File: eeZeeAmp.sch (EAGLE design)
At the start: 18 parts, among them IC1 LM386

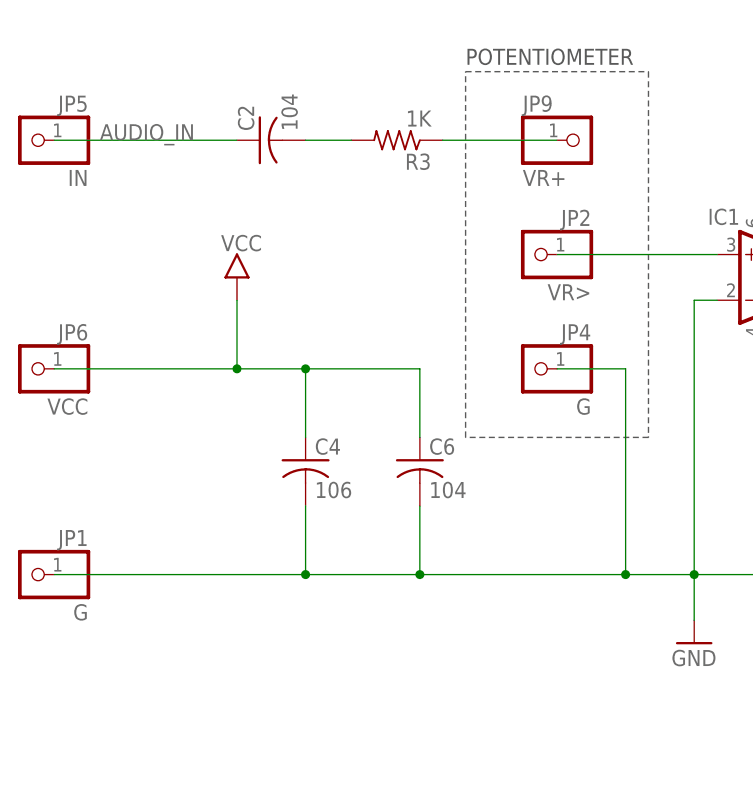
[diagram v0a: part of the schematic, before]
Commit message: Added another ground pin, rearrange layout
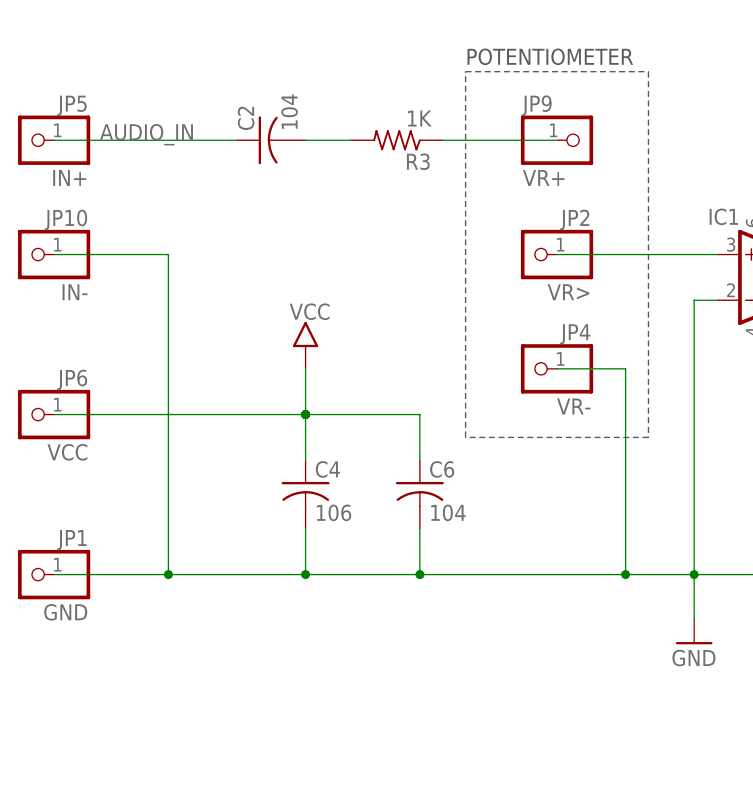
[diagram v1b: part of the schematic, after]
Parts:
- added JP10: IN-, pinhead-2:PINHD-1X01_2.54-S
- JP1: value G -> GND
- JP4: value G -> VR-
- JP5: value IN -> IN+
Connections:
- net GND: now also JP10.1
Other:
- moved on the sheet: C4, C6, JP6
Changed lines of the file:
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@@
 <part name="FRAME1" library="bt" deviceset="LETTER_L" device=""/>
 <part name="C6" library="rcl" deviceset="C-US" device="C0603" value="104"/>
-<part name="JP5" library="pinhead-2" deviceset="PINHD-1X01" device="_2.54-S" value="IN"/>
+<part name="JP5" library="pinhead-2" deviceset="PINHD-1X01" device="_2.54-S" value="IN+"/>
 <part name="JP6" library="pinhead-2" deviceset="PINHD-1X01" device="_2.54-S" value="VCC"/>
 <part name="JP7" library="pinhead-2" deviceset="PINHD-1X01" device="_2.54-S" value="SP+"/>
-<part name="JP1" library="pinhead-2" deviceset="PINHD-1X01" device="_2.54-S" value="G"/>
+<part name="JP1" library="pinhead-2" deviceset="PINHD-1X01" device="_2.54-S" value="GND"/>
 <part name="JP3" library="pinhead-2" deviceset="PINHD-1X01" device="_2.54-S" value="G1"/>
 <part name="JP8" library="pinhead-2" deviceset="PINHD-1X01" device="_2.54-S" value="G8"/>
-<part name="JP4" library="pinhead-2" deviceset="PINHD-1X01" device="_2.54-S" value="G"/>
+<part name="JP4" library="pinhead-2" deviceset="PINHD-1X01" device="_2.54-S" value="VR-"/>
 <part name="JP2" library="pinhead-2" deviceset="PINHD-1X01" device="_2.54-S" value="VR&gt;"/>
 <part name="JP9" library="pinhead-2" deviceset="PINHD-1X01" device="_2.54-S" value="VR+"/>
+<part name="JP10" library="pinhead-2" deviceset="PINHD-1X01" device="_2.54-S" value="IN-"/>
 </parts>
 <sheets>
@@
 <instance part="R3" gate="G$1" x="91.44" y="127" rot="R180"/>
 <instance part="U$1" gate="G$1" x="132.08" y="142.24"/>
-<instance part="U$2" gate="G$1" x="73.66" y="109.22"/>
-<instance part="C4" gate="G$1" x="81.28" y="91.44"/>
+<instance part="U$2" gate="G$1" x="81.28" y="101.6"/>
+<instance part="C4" gate="G$1" x="81.28" y="88.9"/>
 <instance part="GND1" gate="1" x="124.46" y="71.12"/>
 <instance part="C5" gate="G$1" x="137.16" y="96.52"/>
 <instance part="FRAME1" gate="G$1" x="0" y="0"/>
 <instance part="FRAME1" gate="G$2" x="147.32" y="2.54"/>
-<instance part="C6" gate="G$1" x="93.98" y="91.44"/>
+<instance part="C6" gate="G$1" x="93.98" y="88.9"/>
 <instance part="JP5" gate="A" x="50.8" y="127" rot="MR0"/>
-<instance part="JP6" gate="A" x="50.8" y="101.6" rot="MR0"/>
+<instance part="JP6" gate="A" x="50.8" y="96.52" rot="MR0"/>
 <instance part="JP7" gate="A" x="190.5" y="111.76"/>
 <instance part="JP1" gate="A" x="50.8" y="78.74" rot="MR0"/>
@@
 <instance part="JP2" gate="A" x="106.68" y="114.3" rot="MR0"/>
 <instance part="JP9" gate="A" x="111.76" y="127"/>
+<instance part="JP10" gate="A" x="50.8" y="114.3" rot="MR0"/>
 </instances>
 <busses>
@@
 </segment>
 <segment>
-<wire x1="73.66" y1="101.6" x2="73.66" y2="109.22" width="0.1524" layer="91"/>
+<wire x1="81.28" y1="96.52" x2="81.28" y2="101.6" width="0.1524" layer="91"/>
 <pinref part="U$2" gate="G$1" pin="VCC"/>
-<wire x1="53.34" y1="101.6" x2="73.66" y2="101.6" width="0.1524" layer="91"/>
+<wire x1="53.34" y1="96.52" x2="81.28" y2="96.52" width="0.1524" layer="91"/>
 <pinref part="C4" gate="G$1" pin="1"/>
-<wire x1="73.66" y1="101.6" x2="81.28" y2="101.6" width="0.1524" layer="91"/>
-<wire x1="81.28" y1="101.6" x2="81.28" y2="93.98" width="0.1524" layer="91"/>
-<junction x="73.66" y="101.6"/>
+<wire x1="81.28" y1="96.52" x2="81.28" y2="91.44" width="0.1524" layer="91"/>
+<junction x="81.28" y="96.52"/>
 <pinref part="C6" gate="G$1" pin="1"/>
-<wire x1="93.98" y1="93.98" x2="93.98" y2="101.6" width="0.1524" layer="91"/>
-<wire x1="93.98" y1="101.6" x2="81.28" y2="101.6" width="0.1524" layer="91"/>
-<junction x="81.28" y="101.6"/>
+<wire x1="93.98" y1="91.44" x2="93.98" y2="96.52" width="0.1524" layer="91"/>
+<wire x1="93.98" y1="96.52" x2="81.28" y2="96.52" width="0.1524" layer="91"/>
+<junction x="81.28" y="96.52"/>
 <pinref part="JP6" gate="A" pin="1"/>
 </segment>
@@
 <wire x1="124.46" y1="109.22" x2="124.46" y2="78.74" width="0.1524" layer="91"/>
 <junction x="124.46" y="78.74"/>
-<wire x1="53.34" y1="78.74" x2="81.28" y2="78.74" width="0.1524" layer="91"/>
+<wire x1="53.34" y1="78.74" x2="66.04" y2="78.74" width="0.1524" layer="91"/>
 <pinref part="C4" gate="G$1" pin="2"/>
+<wire x1="66.04" y1="78.74" x2="81.28" y2="78.74" width="0.1524" layer="91"/>
 <wire x1="81.28" y1="78.74" x2="93.98" y2="78.74" width="0.1524" layer="91"/>
 <wire x1="93.98" y1="78.74" x2="116.84" y2="78.74" width="0.1524" layer="91"/>
 <wire x1="116.84" y1="78.74" x2="124.46" y2="78.74" width="0.1524" layer="91"/>
-<wire x1="81.28" y1="86.36" x2="81.28" y2="78.74" width="0.1524" layer="91"/>
+<wire x1="81.28" y1="83.82" x2="81.28" y2="78.74" width="0.1524" layer="91"/>
 <junction x="81.28" y="78.74"/>
 <pinref part="GND1" gate="1" pin="GND"/>
@@
 <junction x="137.16" y="78.74"/>
 <pinref part="C6" gate="G$1" pin="2"/>
-<wire x1="93.98" y1="86.36" x2="93.98" y2="78.74" width="0.1524" layer="91"/>
+<wire x1="93.98" y1="83.82" x2="93.98" y2="78.74" width="0.1524" layer="91"/>
 <junction x="93.98" y="78.74"/>
 <pinref part="JP1" gate="A" pin="1"/>
@@
 <wire x1="116.84" y1="101.6" x2="116.84" y2="78.74" width="0.1524" layer="91"/>
 <junction x="116.84" y="78.74"/>
+<pinref part="JP10" gate="A" pin="1"/>
+<wire x1="53.34" y1="114.3" x2="66.04" y2="114.3" width="0.1524" layer="91"/>
+<wire x1="66.04" y1="114.3" x2="66.04" y2="78.74" width="0.1524" layer="91"/>
+<junction x="66.04" y="78.74"/>
 </segment>
 </net>

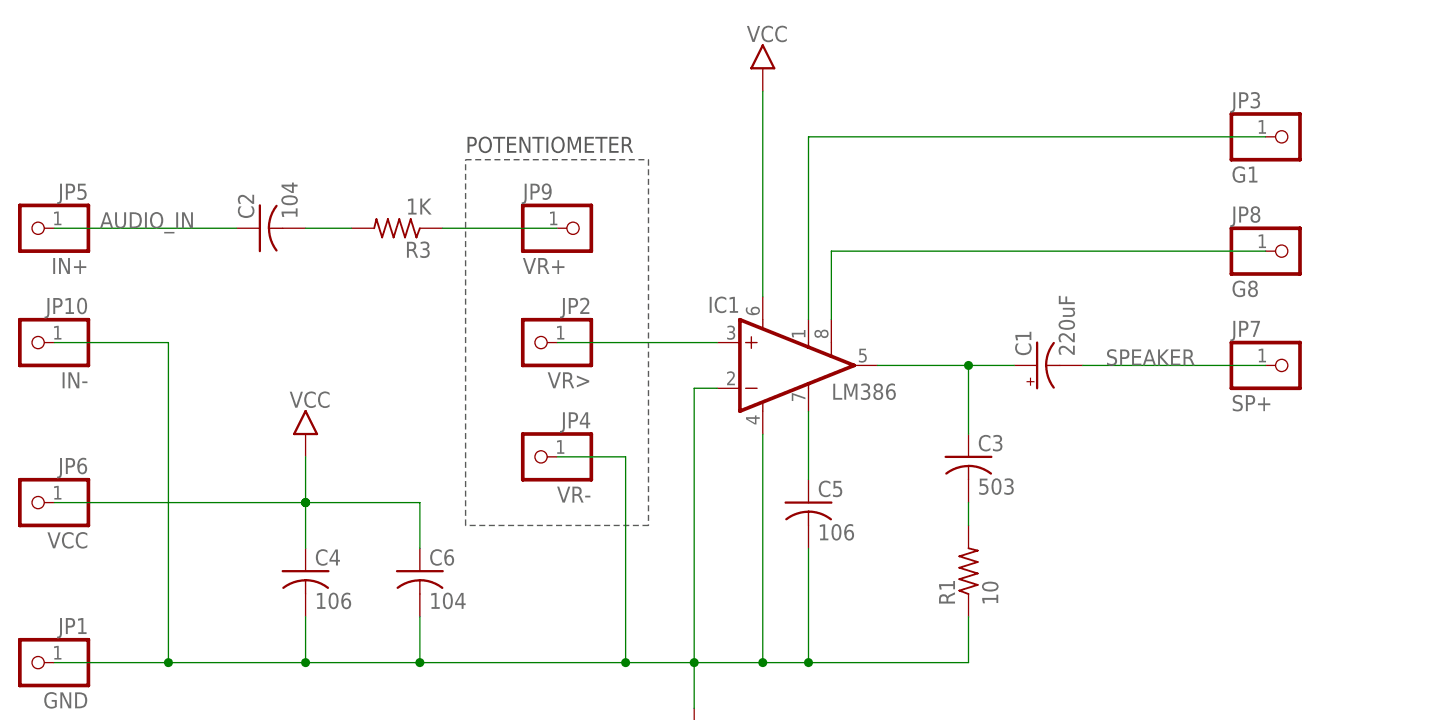
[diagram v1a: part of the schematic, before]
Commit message: moved label
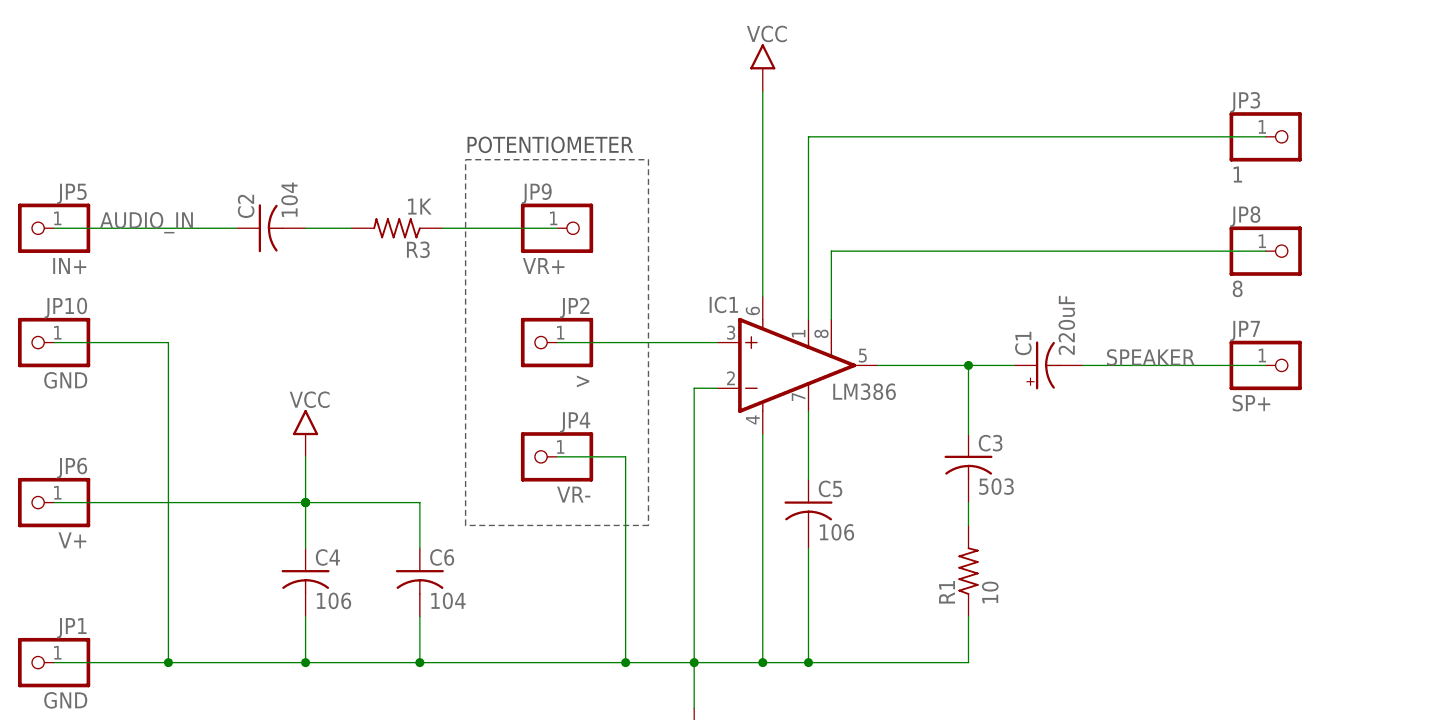
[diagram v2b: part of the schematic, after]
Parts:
- JP10: value IN- -> GND
- JP2: value VR> -> >
- JP3: value G1 -> 1
- JP6: value VCC -> V+
- JP8: value G8 -> 8
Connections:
- net G1 renamed 1
- net G8 renamed 8
- net N$1 renamed 3
- net N$3 renamed 5
- net N$7 renamed 7
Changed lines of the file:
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@@
 <part name="C6" library="rcl" deviceset="C-US" device="C0603" value="104"/>
 <part name="JP5" library="pinhead-2" deviceset="PINHD-1X01" device="_2.54-S" value="IN+"/>
-<part name="JP6" library="pinhead-2" deviceset="PINHD-1X01" device="_2.54-S" value="VCC"/>
+<part name="JP6" library="pinhead-2" deviceset="PINHD-1X01" device="_2.54-S" value="V+"/>
 <part name="JP7" library="pinhead-2" deviceset="PINHD-1X01" device="_2.54-S" value="SP+"/>
 <part name="JP1" library="pinhead-2" deviceset="PINHD-1X01" device="_2.54-S" value="GND"/>
-<part name="JP3" library="pinhead-2" deviceset="PINHD-1X01" device="_2.54-S" value="G1"/>
-<part name="JP8" library="pinhead-2" deviceset="PINHD-1X01" device="_2.54-S" value="G8"/>
+<part name="JP3" library="pinhead-2" deviceset="PINHD-1X01" device="_2.54-S" value="1"/>
+<part name="JP8" library="pinhead-2" deviceset="PINHD-1X01" device="_2.54-S" value="8"/>
 <part name="JP4" library="pinhead-2" deviceset="PINHD-1X01" device="_2.54-S" value="VR-"/>
-<part name="JP2" library="pinhead-2" deviceset="PINHD-1X01" device="_2.54-S" value="VR&gt;"/>
+<part name="JP2" library="pinhead-2" deviceset="PINHD-1X01" device="_2.54-S" value="&gt;"/>
 <part name="JP9" library="pinhead-2" deviceset="PINHD-1X01" device="_2.54-S" value="VR+"/>
-<part name="JP10" library="pinhead-2" deviceset="PINHD-1X01" device="_2.54-S" value="IN-"/>
+<part name="JP10" library="pinhead-2" deviceset="PINHD-1X01" device="_2.54-S" value="GND"/>
 </parts>
 <sheets>
@@
 </busses>
 <nets>
-<net name="N$1" class="0">
+<net name="3" class="0">
 <segment>
 <pinref part="IC1" gate="G$1" pin="+IN"/>
@@
 </segment>
 </net>
-<net name="N$3" class="0">
+<net name="5" class="0">
 <segment>
 <pinref part="C1" gate="G$1" pin="+"/>
@@
 </segment>
 </net>
-<net name="G1" class="0">
+<net name="1" class="0">
 <segment>
 <pinref part="IC1" gate="G$1" pin="GAIN@1"/>
@@
 </segment>
 </net>
-<net name="G8" class="0">
+<net name="8" class="0">
 <segment>
 <pinref part="IC1" gate="G$1" pin="GAIN@2"/>
@@
 </segment>
 </net>
-<net name="N$7" class="0">
+<net name="7" class="0">
 <segment>
 <pinref part="IC1" gate="G$1" pin="BYPASS"/>
